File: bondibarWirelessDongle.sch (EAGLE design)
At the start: 4 parts

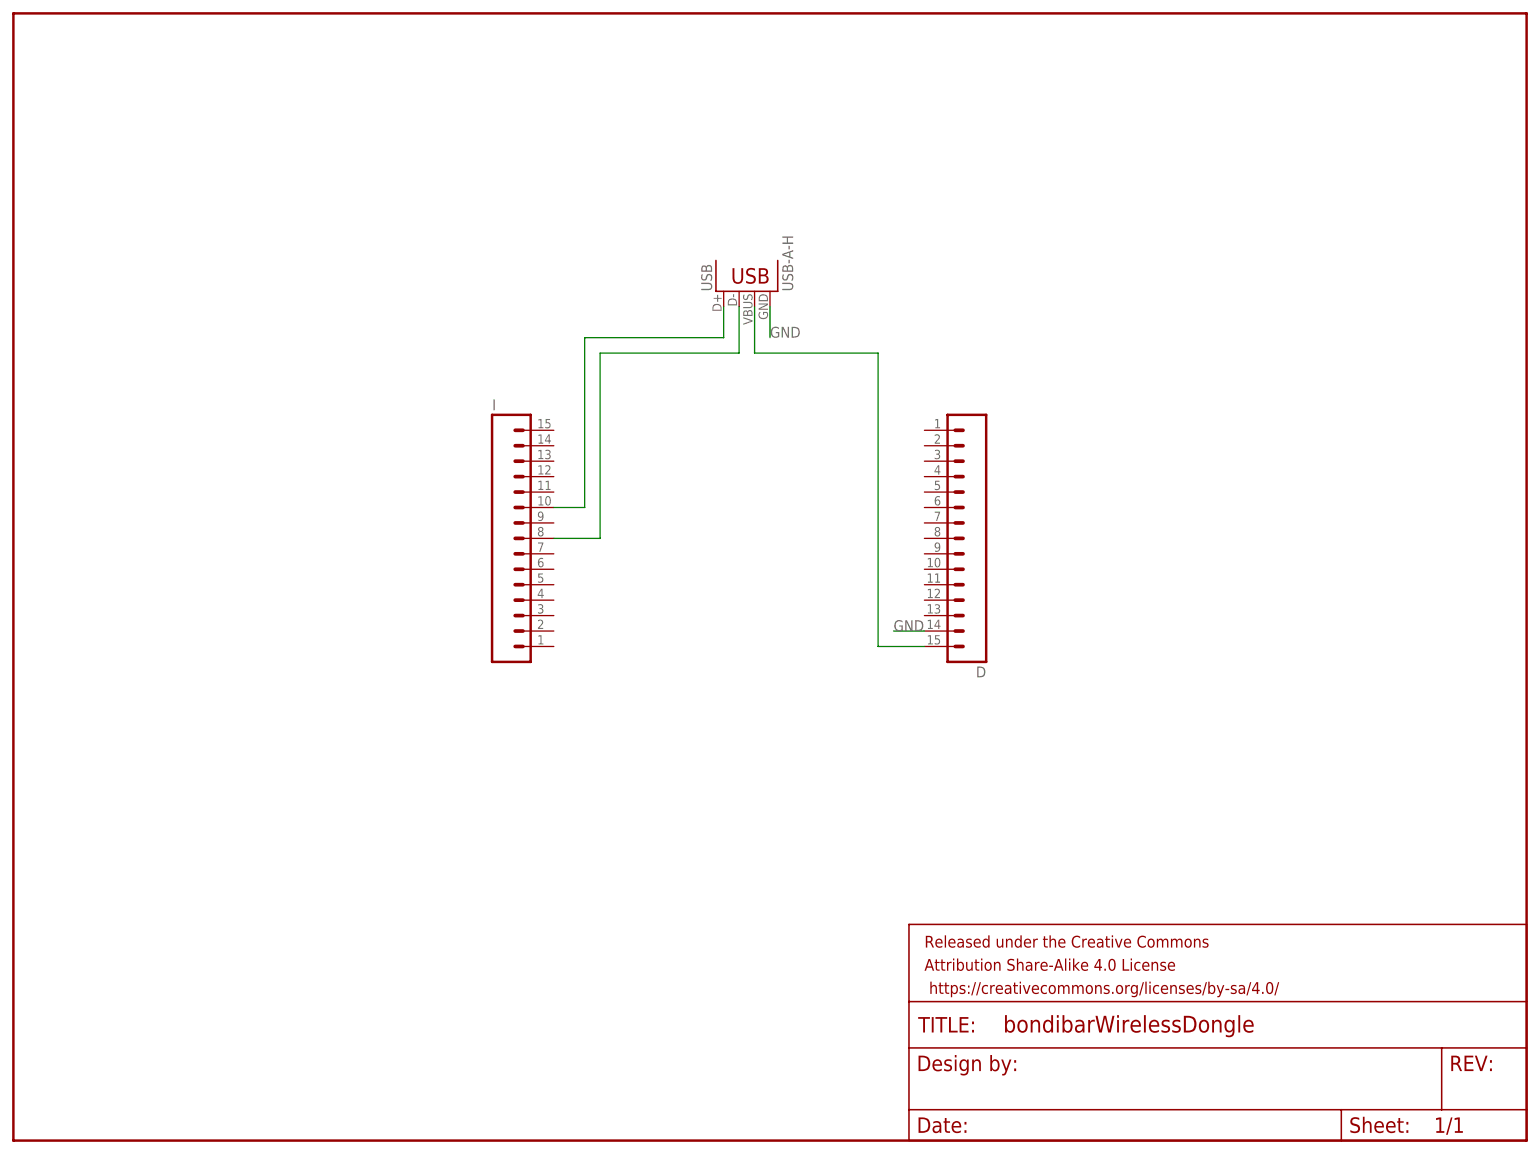
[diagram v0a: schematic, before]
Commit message: Modified version to print in Seedstudio./
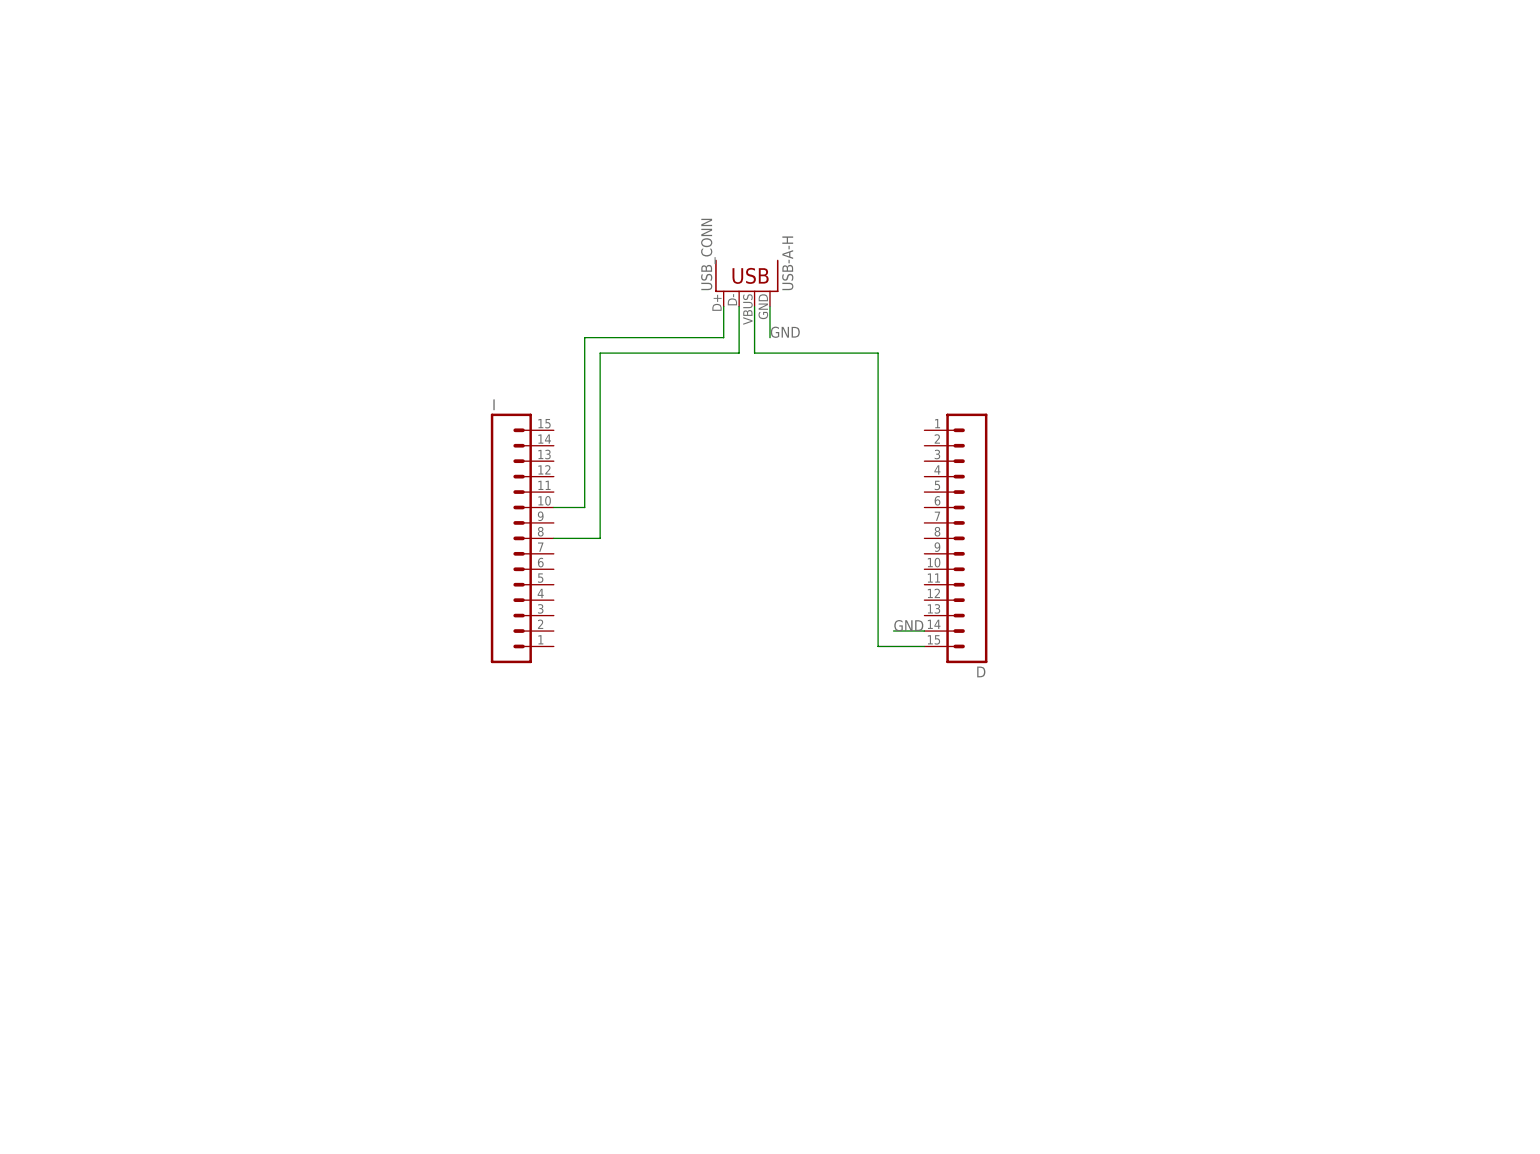
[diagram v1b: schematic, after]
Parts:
- removed FRAME1: FRAME-LETTERNO_PACKAGE, SparkFun-Aesthetics:FRAME-LETTERNO_PACKAGE
- renumbered USB to USB_CONN
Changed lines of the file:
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@@
 </classes>
 <parts>
-<part name="FRAME1" library="SparkFun-Aesthetics" deviceset="FRAME-LETTER" device="NO_PACKAGE"/>
 <part name="D" library="SparkFun-Connectors" deviceset="M15" device=""/>
 <part name="I" library="SparkFun-Connectors" deviceset="M15" device=""/>
-<part name="USB" library="SparkFun-Connectors" deviceset="USB" device="-A-H"/>
+<part name="USB_CONN" library="SparkFun-Connectors" deviceset="USB" device="-A-H"/>
 </parts>
 <sheets>
@@
 </plain>
 <instances>
-<instance part="FRAME1" gate="G$1" x="0" y="0"/>
-<instance part="FRAME1" gate="V" x="147.32" y="0"/>
 <instance part="D" gate="G$1" x="160.02" y="99.06" rot="R180"/>
 <instance part="I" gate="G$1" x="78.74" y="99.06"/>
-<instance part="USB" gate="G$1" x="124.46" y="139.7" rot="R90"/>
+<instance part="USB_CONN" gate="G$1" x="124.46" y="139.7" rot="R90"/>
 </instances>
 <busses>
@@
 <wire x1="93.98" y1="104.14" x2="93.98" y2="132.08" width="0.1524" layer="91"/>
 <wire x1="93.98" y1="132.08" x2="116.84" y2="132.08" width="0.1524" layer="91"/>
-<pinref part="USB" gate="G$1" pin="D+"/>
+<pinref part="USB_CONN" gate="G$1" pin="D+"/>
 <wire x1="116.84" y1="132.08" x2="116.84" y2="137.16" width="0.1524" layer="91"/>
 </segment>
@@
 <net name="N$4" class="0">
 <segment>
-<pinref part="USB" gate="G$1" pin="D-"/>
+<pinref part="USB_CONN" gate="G$1" pin="D-"/>
 <wire x1="119.38" y1="137.16" x2="119.38" y2="129.54" width="0.1524" layer="91"/>
 <wire x1="119.38" y1="129.54" x2="96.52" y2="129.54" width="0.1524" layer="91"/>
@@
 <net name="N$2" class="0">
 <segment>
-<pinref part="USB" gate="G$1" pin="VBUS"/>
+<pinref part="USB_CONN" gate="G$1" pin="VBUS"/>
 <wire x1="121.92" y1="137.16" x2="121.92" y2="129.54" width="0.1524" layer="91"/>
 <wire x1="121.92" y1="129.54" x2="142.24" y2="129.54" width="0.1524" layer="91"/>
@@
 <net name="GND" class="0">
 <segment>
-<pinref part="USB" gate="G$1" pin="GND"/>
+<pinref part="USB_CONN" gate="G$1" pin="GND"/>
 <wire x1="124.46" y1="137.16" x2="124.46" y2="132.08" width="0.1524" layer="91"/>
 <label x="124.46" y="132.08" size="1.778" layer="95"/>

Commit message: v0.4 - Seedstudio printed version
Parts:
- renumbered USB_CONN to DATA_OUT
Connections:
- net GND: now also D.10, I.14, I.7
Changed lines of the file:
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@@
 <part name="D" library="SparkFun-Connectors" deviceset="M15" device=""/>
 <part name="I" library="SparkFun-Connectors" deviceset="M15" device=""/>
-<part name="USB_CONN" library="SparkFun-Connectors" deviceset="USB" device="-A-H"/>
+<part name="DATA_OUT" library="SparkFun-Connectors" deviceset="USB" device="-A-H"/>
 </parts>
 <sheets>
@@
 <instance part="D" gate="G$1" x="160.02" y="99.06" rot="R180"/>
 <instance part="I" gate="G$1" x="78.74" y="99.06"/>
-<instance part="USB_CONN" gate="G$1" x="124.46" y="139.7" rot="R90"/>
+<instance part="DATA_OUT" gate="G$1" x="124.46" y="139.7" rot="R90"/>
 </instances>
 <busses>
@@
 <wire x1="93.98" y1="104.14" x2="93.98" y2="132.08" width="0.1524" layer="91"/>
 <wire x1="93.98" y1="132.08" x2="116.84" y2="132.08" width="0.1524" layer="91"/>
-<pinref part="USB_CONN" gate="G$1" pin="D+"/>
+<pinref part="DATA_OUT" gate="G$1" pin="D+"/>
 <wire x1="116.84" y1="132.08" x2="116.84" y2="137.16" width="0.1524" layer="91"/>
 </segment>
@@
 <net name="N$4" class="0">
 <segment>
-<pinref part="USB_CONN" gate="G$1" pin="D-"/>
+<pinref part="DATA_OUT" gate="G$1" pin="D-"/>
 <wire x1="119.38" y1="137.16" x2="119.38" y2="129.54" width="0.1524" layer="91"/>
 <wire x1="119.38" y1="129.54" x2="96.52" y2="129.54" width="0.1524" layer="91"/>
@@
 <net name="N$2" class="0">
 <segment>
-<pinref part="USB_CONN" gate="G$1" pin="VBUS"/>
+<pinref part="DATA_OUT" gate="G$1" pin="VBUS"/>
 <wire x1="121.92" y1="137.16" x2="121.92" y2="129.54" width="0.1524" layer="91"/>
 <wire x1="121.92" y1="129.54" x2="142.24" y2="129.54" width="0.1524" layer="91"/>
@@
 <net name="GND" class="0">
 <segment>
-<pinref part="USB_CONN" gate="G$1" pin="GND"/>
+<pinref part="DATA_OUT" gate="G$1" pin="GND"/>
 <wire x1="124.46" y1="137.16" x2="124.46" y2="132.08" width="0.1524" layer="91"/>
 <label x="124.46" y="132.08" size="1.778" layer="95"/>
@@
 <label x="144.78" y="83.82" size="1.778" layer="95"/>
 </segment>
+<segment>
+<pinref part="I" gate="G$1" pin="7"/>
+<wire x1="88.9" y1="96.52" x2="96.52" y2="96.52" width="0.1524" layer="91"/>
+<label x="96.52" y="96.52" size="1.778" layer="95"/>
+</segment>
+<segment>
+<pinref part="I" gate="G$1" pin="14"/>
+<wire x1="88.9" y1="114.3" x2="91.44" y2="114.3" width="0.1524" layer="91"/>
+<label x="91.44" y="114.3" size="1.778" layer="95"/>
+</segment>
+<segment>
+<pinref part="D" gate="G$1" pin="10"/>
+<wire x1="149.86" y1="93.98" x2="144.78" y2="93.98" width="0.1524" layer="91"/>
+<label x="142.24" y="93.98" size="1.778" layer="95"/>
+</segment>
 </net>
